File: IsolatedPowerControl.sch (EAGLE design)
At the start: 38 parts, among them IC1 LM358, K2 G2RATE-OJ, Q1 FDN360P, U1 MCP23008-E/SO, U2 MCP4716A0T-E/CH

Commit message: Initial fit (incomplete routing)
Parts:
- removed D2: P6KEXXCTS-P6KE, diode:P6KEXXCTS-P6KE
- removed K2: G2RATE-OJ, relay:G2RATE-OJ
- removed LED2: (no value), led:LED5MM
- removed R13: 270, rcl:R-EU_R0805
- added JP1, JP3, JP6, JP7, JP8: (no value), pinhead:PINHD-1X1
- JP4: device pinhead:PINHD-1X7 -> pinhead:PINHD-1X1
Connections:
- removed net N$10: JP4.7, K22.S
- removed net N$8: LED2.C, R13.2
- removed net N$9: JP4.6, K22.P
- net DIRECTONOFF_BUFFERED: now also JP7.1; no longer JP4.5
- net N$13: now also JP8.1; no longer JP4.1
- net N$18: now also JP1.1; no longer D2.1, K21.1, R13.1
- net N$3: now also JP3.1; no longer JP4.2
- net V+: no longer D2.2, K21.2, LED2.A
- net VPOWER: now also JP4.1; no longer JP4.3
- net VPOWER_BUFFERED: now also JP6.1; no longer JP4.4
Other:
- moved on the sheet: D1, Q1, R11, R12, R14, T3

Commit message: First layout complete and checked
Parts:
- JP1, JP3, JP4, JP6, JP7, JP8: device pinhead:PINHD-1X1 -> pinhead:PINHD-1X1LARGEPAD
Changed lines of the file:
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@@
 <part name="JP5" library="pinhead" deviceset="PINHD-1X4" device=""/>
 <part name="JP2" library="pinhead" deviceset="PINHD-1X2" device=""/>
-<part name="JP1" library="pinhead" deviceset="PINHD-1X1" device=""/>
-<part name="JP3" library="pinhead" deviceset="PINHD-1X1" device=""/>
-<part name="JP4" library="pinhead" deviceset="PINHD-1X1" device=""/>
-<part name="JP6" library="pinhead" deviceset="PINHD-1X1" device=""/>
-<part name="JP7" library="pinhead" deviceset="PINHD-1X1" device=""/>
-<part name="JP8" library="pinhead" deviceset="PINHD-1X1" device=""/>
+<part name="JP1" library="pinhead" deviceset="PINHD-1X1" device="LARGEPAD"/>
+<part name="JP3" library="pinhead" deviceset="PINHD-1X1" device="LARGEPAD"/>
+<part name="JP4" library="pinhead" deviceset="PINHD-1X1" device="LARGEPAD"/>
+<part name="JP6" library="pinhead" deviceset="PINHD-1X1" device="LARGEPAD"/>
+<part name="JP7" library="pinhead" deviceset="PINHD-1X1" device="LARGEPAD"/>
+<part name="JP8" library="pinhead" deviceset="PINHD-1X1" device="LARGEPAD"/>
 </parts>
 <sheets>
@@
 </segment>
 <segment>
-<wire x1="347.98" y1="-40.64" x2="322.58" y2="-40.64" width="0.1524" layer="91"/>
-<label x="322.58" y="-40.64" size="1.778" layer="95"/>
+<wire x1="347.98" y1="-40.64" x2="312.42" y2="-40.64" width="0.1524" layer="91"/>
+<label x="312.42" y="-40.64" size="1.778" layer="95"/>
 <pinref part="JP4" gate="G$1" pin="1"/>
 </segment>
@@
 <net name="VPOWER_BUFFERED" class="0">
 <segment>
-<label x="322.58" y="-43.18" size="1.778" layer="95"/>
-<wire x1="347.98" y1="-43.18" x2="322.58" y2="-43.18" width="0.1524" layer="91"/>
+<label x="312.42" y="-43.18" size="1.778" layer="95"/>
+<wire x1="347.98" y1="-43.18" x2="312.42" y2="-43.18" width="0.1524" layer="91"/>
 <pinref part="JP6" gate="G$1" pin="1"/>
 </segment>
 <segment>
-<wire x1="309.88" y1="-73.66" x2="317.5" y2="-73.66" width="0.1524" layer="91"/>
+<label x="332.74" y="-73.66" size="1.778" layer="95"/>
+<wire x1="317.5" y1="-73.66" x2="358.14" y2="-73.66" width="0.1524" layer="91"/>
+<pinref part="IC1" gate="B" pin="OUT"/>
+<wire x1="317.5" y1="-73.66" x2="309.88" y2="-73.66" width="0.1524" layer="91"/>
 <wire x1="317.5" y1="-73.66" x2="317.5" y2="-83.82" width="0.1524" layer="91"/>
+<junction x="317.5" y="-73.66"/>
 <wire x1="317.5" y1="-83.82" x2="292.1" y2="-83.82" width="0.1524" layer="91"/>
 <wire x1="292.1" y1="-83.82" x2="292.1" y2="-76.2" width="0.1524" layer="91"/>
+<pinref part="IC1" gate="B" pin="-IN"/>
 <wire x1="292.1" y1="-76.2" x2="294.64" y2="-76.2" width="0.1524" layer="91"/>
-<wire x1="317.5" y1="-73.66" x2="355.6" y2="-73.66" width="0.1524" layer="91"/>
-<junction x="317.5" y="-73.66"/>
-<label x="322.58" y="-73.66" size="1.778" layer="95"/>
-<pinref part="IC1" gate="B" pin="-IN"/>
-<pinref part="IC1" gate="B" pin="OUT"/>
 </segment>
 </net>
@@
 </segment>
 <segment>
-<wire x1="347.98" y1="-45.72" x2="322.58" y2="-45.72" width="0.1524" layer="91"/>
-<label x="322.58" y="-45.72" size="1.778" layer="95"/>
+<wire x1="347.98" y1="-45.72" x2="312.42" y2="-45.72" width="0.1524" layer="91"/>
+<label x="312.42" y="-45.72" size="1.778" layer="95"/>
 <pinref part="JP7" gate="G$1" pin="1"/>
 </segment>

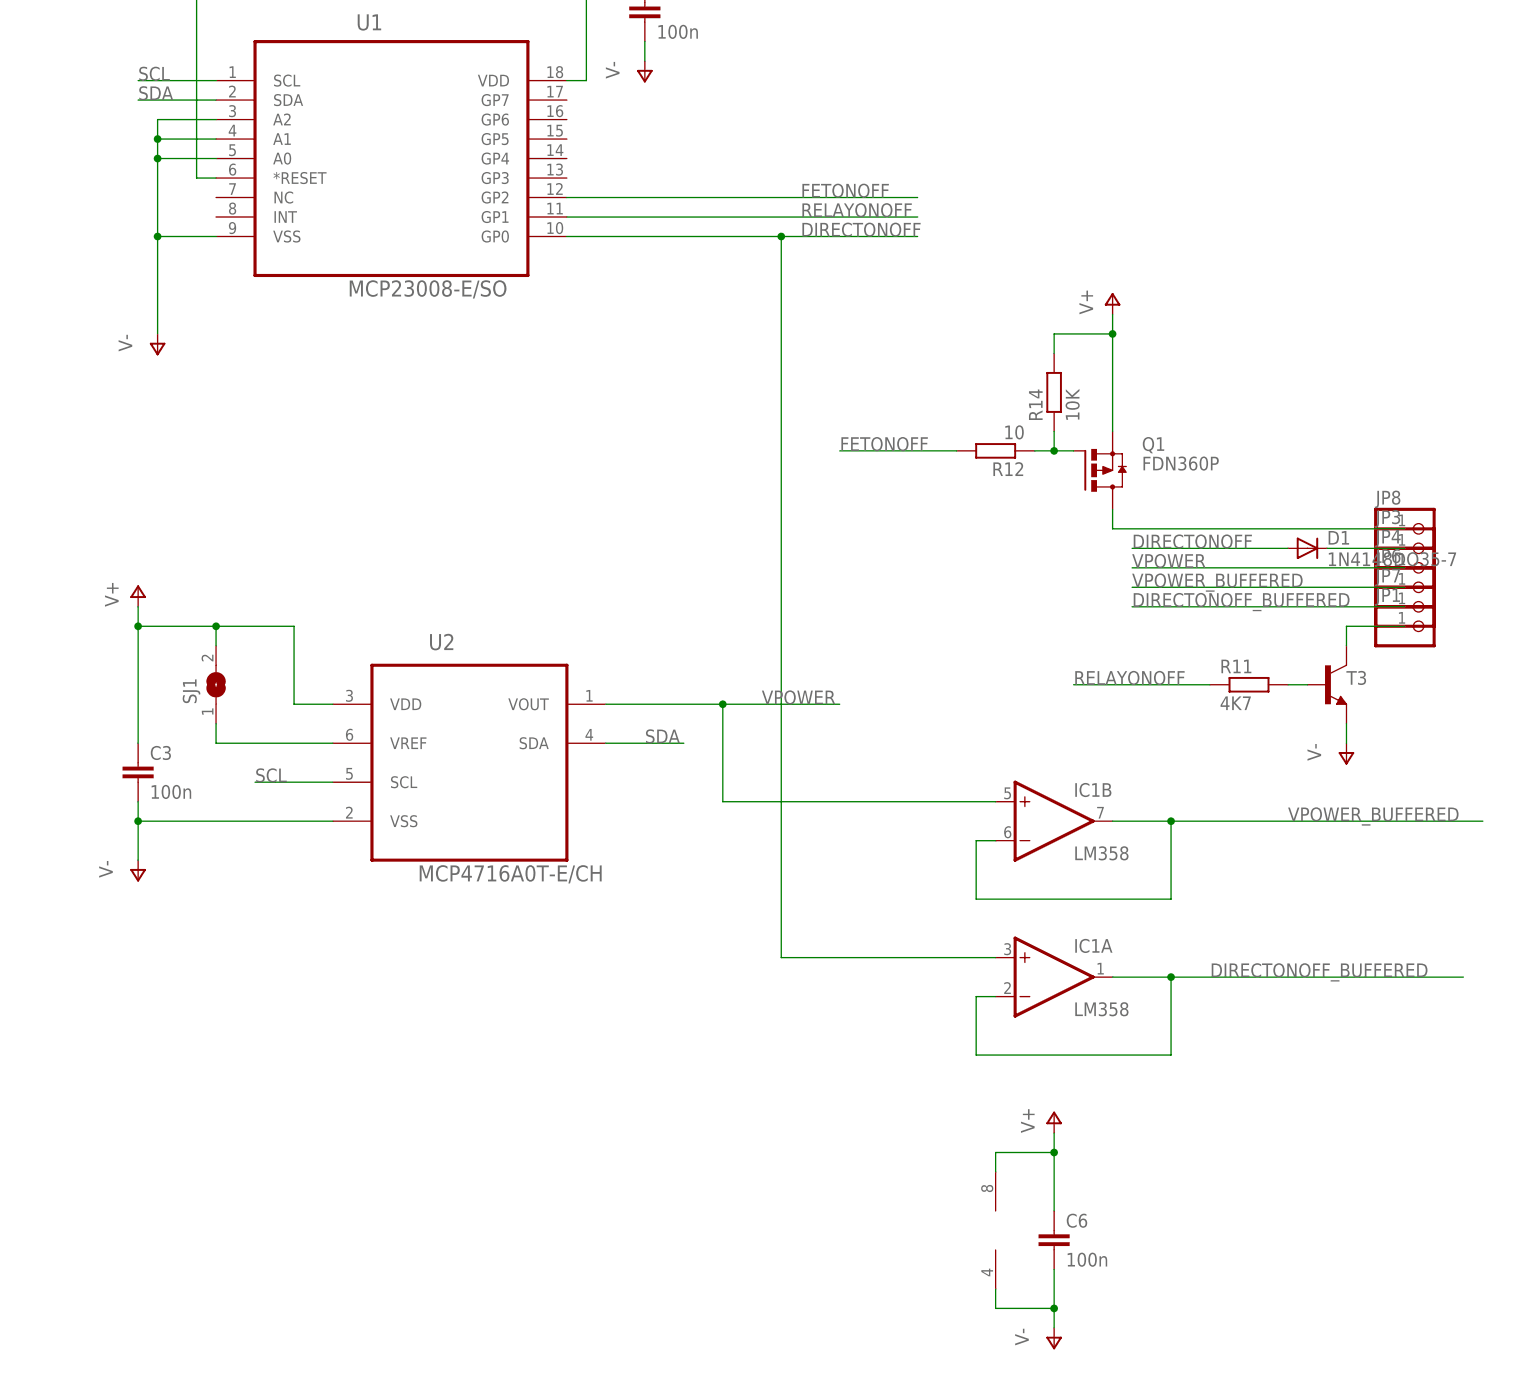
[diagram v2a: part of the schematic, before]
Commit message: Added op amp with enable/power down (MCP6273T) and re-routed.
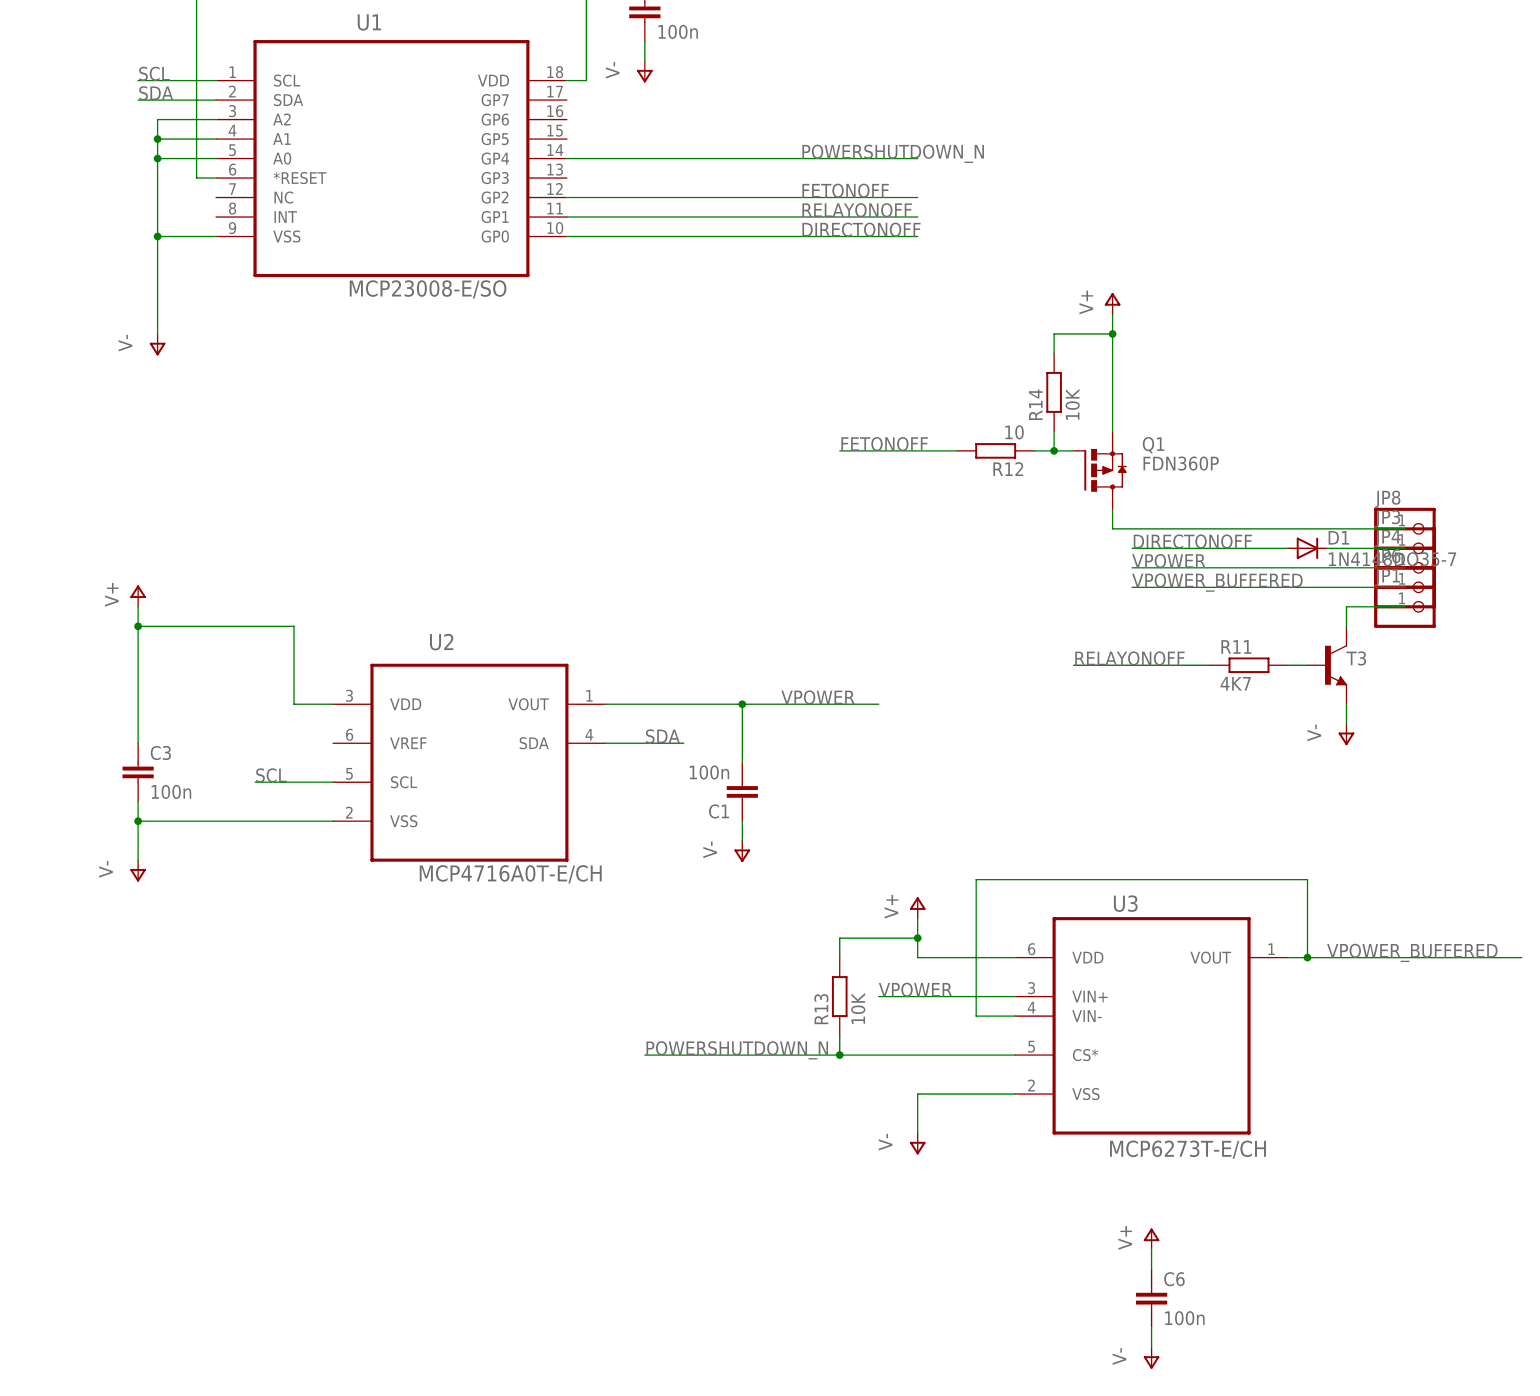
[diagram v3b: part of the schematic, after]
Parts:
- removed IC1: LM358, linear:LM358
- removed JP7: (no value), pinhead:PINHD-1X1LARGEPAD
- removed SJ1: (no value), jumper:SJW
- added C1: 100n, rcl:C-EUC1206K
- added R13: 10K, rcl:R-EU_R0805
- added U3: MCP6273T-E/CH, MCP6273T-ECH:MCP6273T-E/CH
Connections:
- removed net DIRECTONOFF_BUFFERED: IC1A.-IN, IC1A.OUT, JP7.1
- removed net N$11: SJ1.1, U2.VREF
- new net POWERSHUTDOWN_N: R13.1, U1.GP4, U3.CS*
- net DIRECTONOFF: no longer IC1A.+IN
- net V+: now also R13.2, U3.VDD; no longer IC1P.V+, SJ1.2
- net V-: now also C1.1, U3.VSS; no longer IC1P.V-
- net VPOWER: now also C1.2, U3.VIN+; no longer IC1B.+IN
- net VPOWER_BUFFERED: now also U3.VIN-, U3.VOUT; no longer IC1B.-IN, IC1B.OUT
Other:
- moved on the sheet: C6, JP1, R11, T3

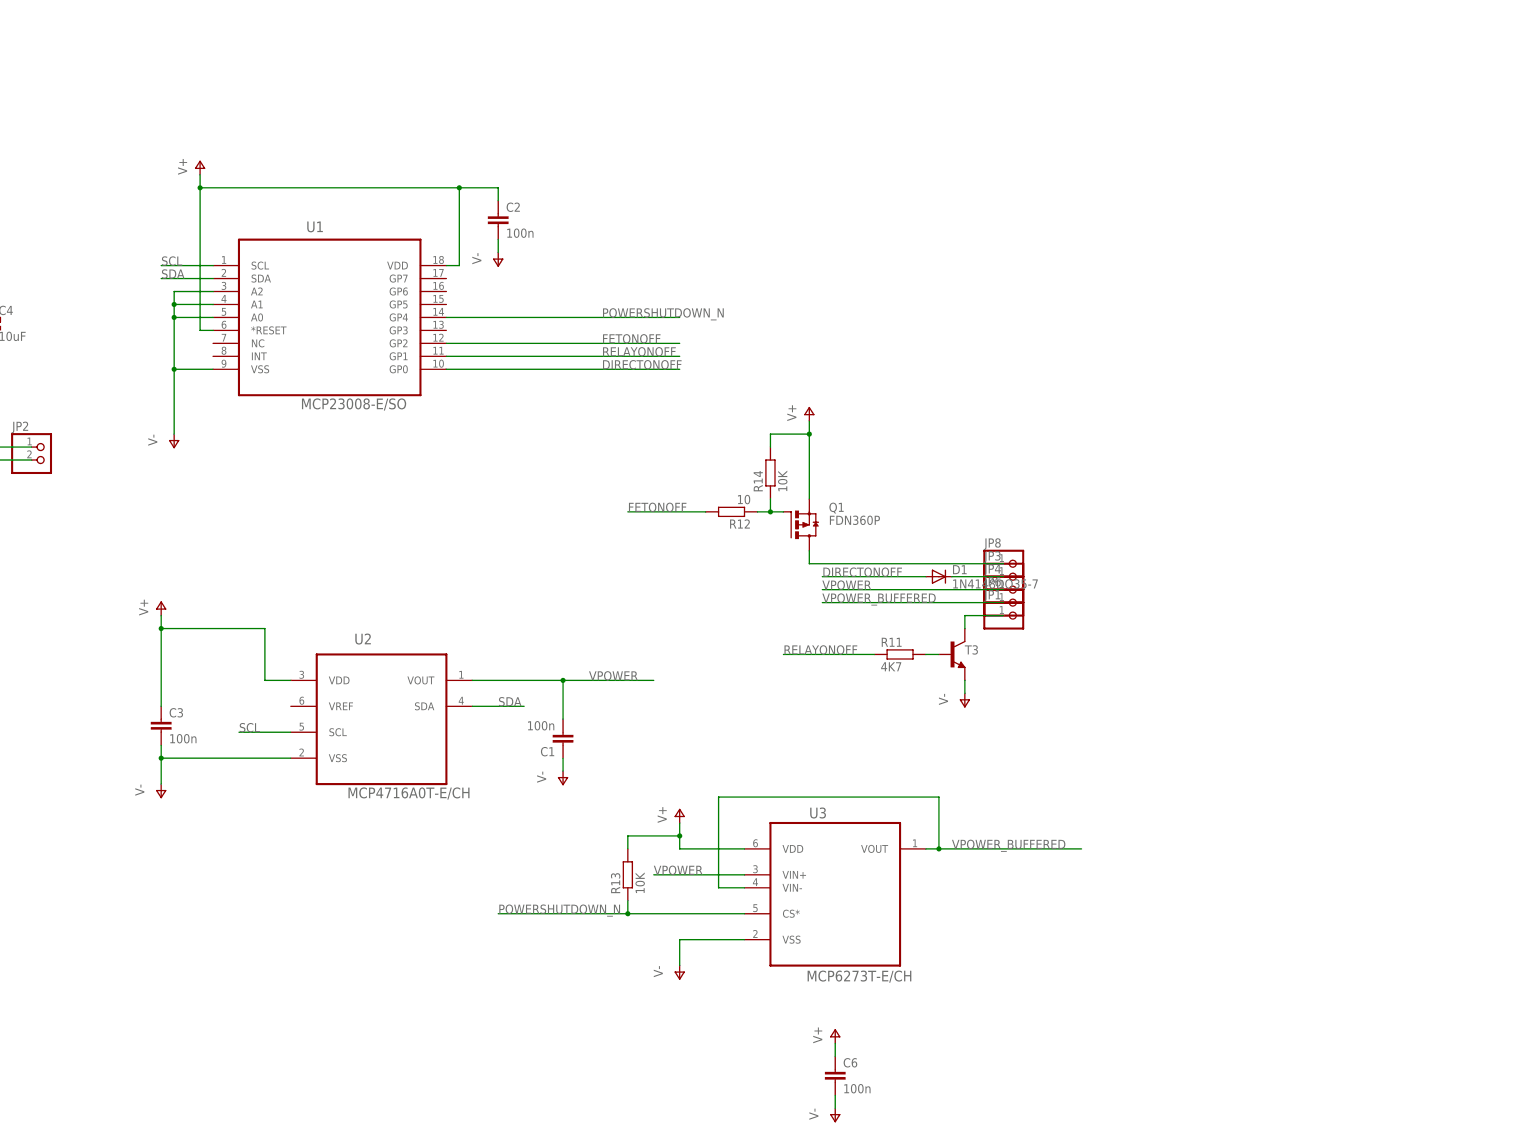
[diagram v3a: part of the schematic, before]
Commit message: Added another isolated aux channel
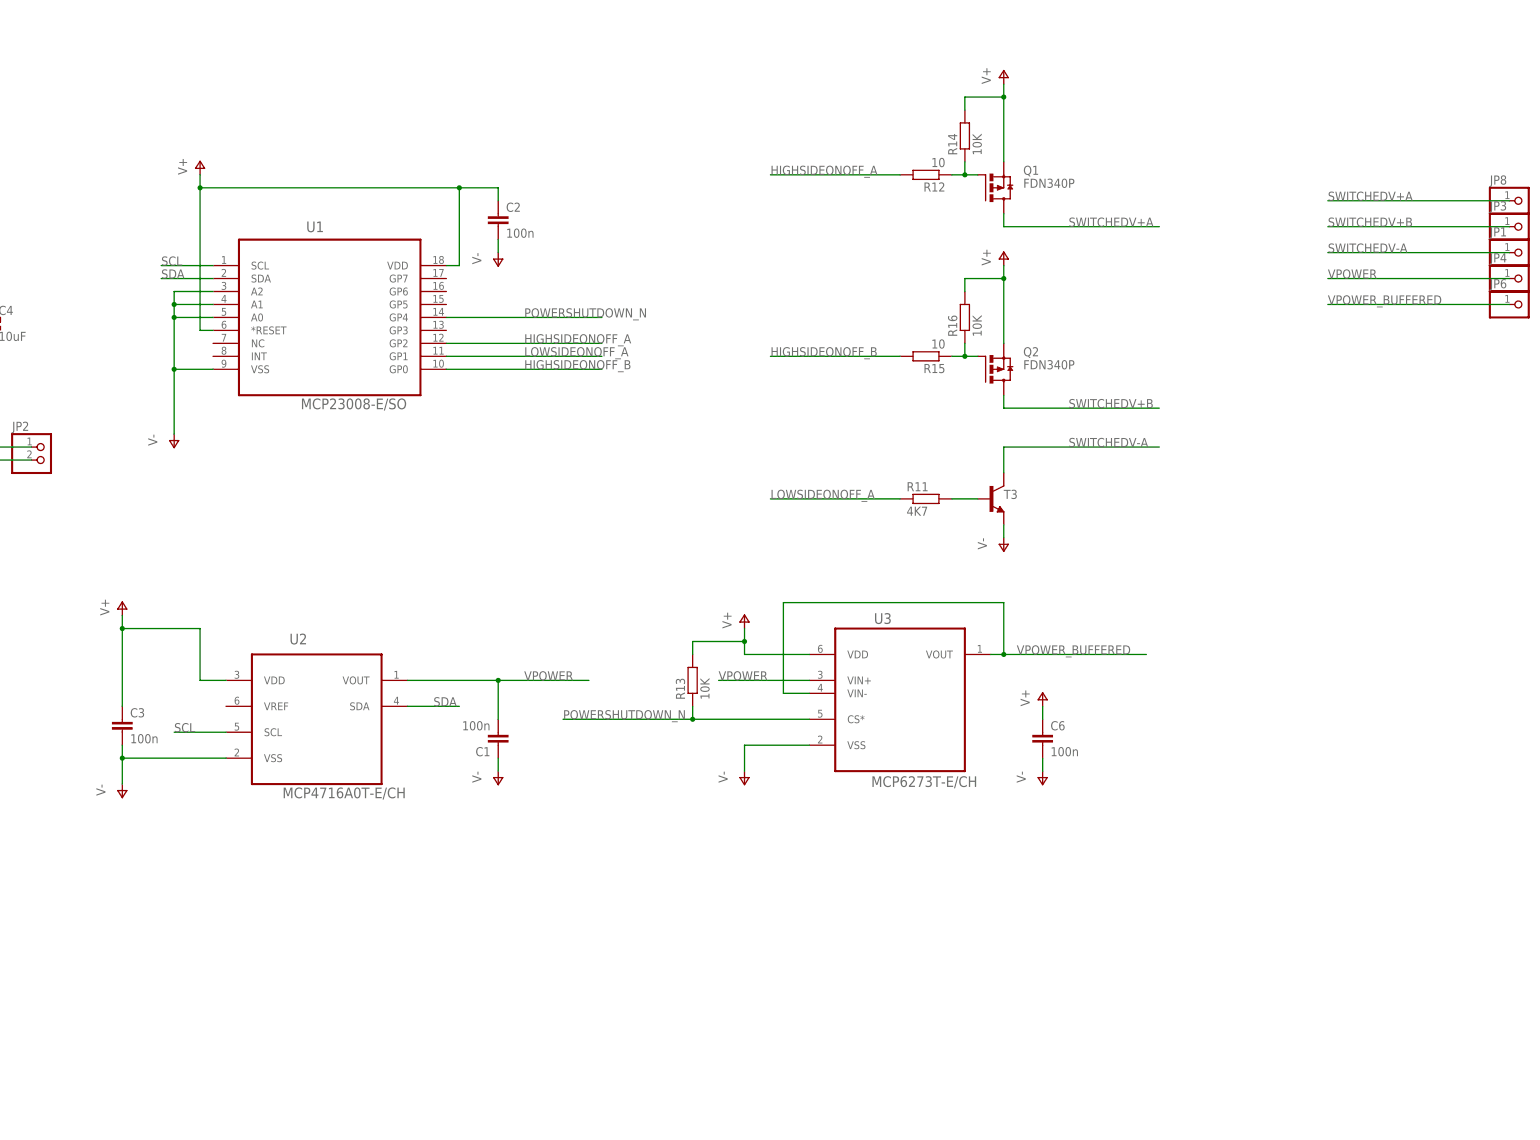
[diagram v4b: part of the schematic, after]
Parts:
- removed D1: 1N4148DO35-7, diode:1N4148DO35-7
- added Q2: FDN340P, transistor-power:FDN360P
- added R15: 10, rcl:R-EU_R0603
- added R16: 10K, rcl:R-EU_R0805
- Q1: value FDN360P -> FDN340P
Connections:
- net FETONOFF renamed HIGHSIDEONOFF_A
- net N$13 renamed SWITCHEDV+A
- net N$18 renamed SWITCHEDV-A
- net RELAYONOFF renamed LOWSIDEONOFF_A
- removed net DIRECTONOFF: D1.A, U1.GP0
- removed net N$3: D1.C, JP3.1
- new net HIGHSIDEONOFF_B: R15.2, U1.GP0
- new net N$8: Q2.G, R15.1, R16.1
- new net SWITCHEDV+B: JP3.1, Q2.D
- net V+: now also Q2.S, R16.2
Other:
- moved on the sheet: C1, C3, C6, JP1, JP3, JP4, JP6, JP8, Q1, R11, R12, R13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
